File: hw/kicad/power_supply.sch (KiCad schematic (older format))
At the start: 23 parts

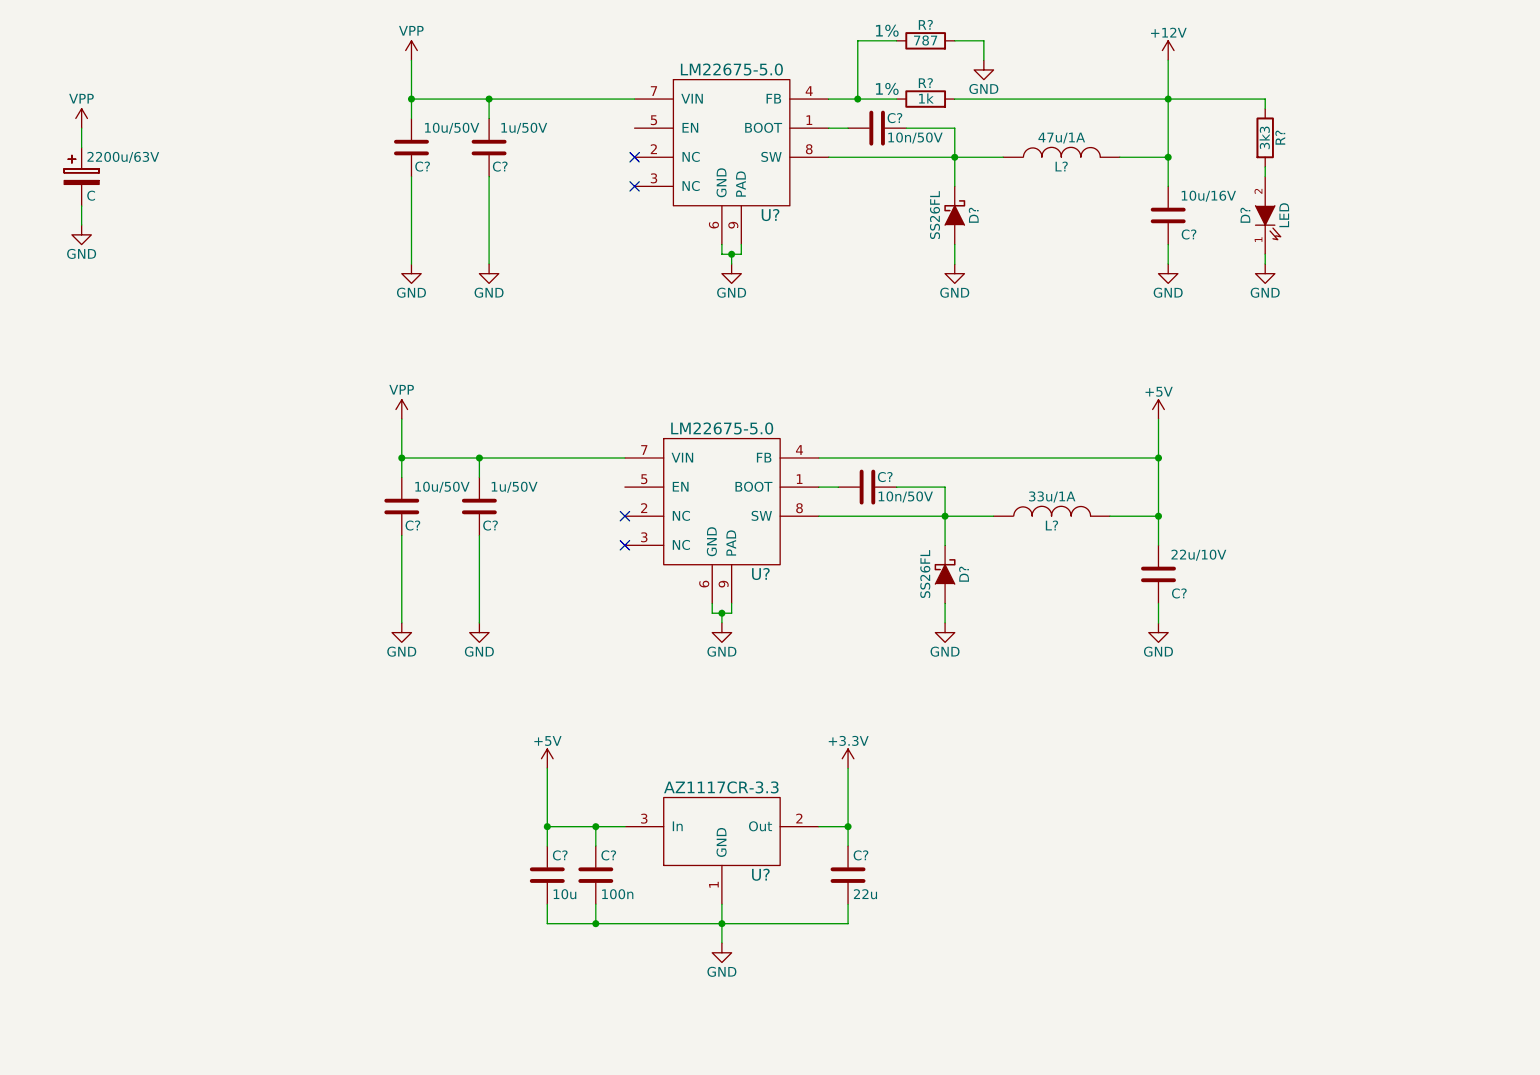
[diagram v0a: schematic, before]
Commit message: Gate power supply enabling and board temp sensor
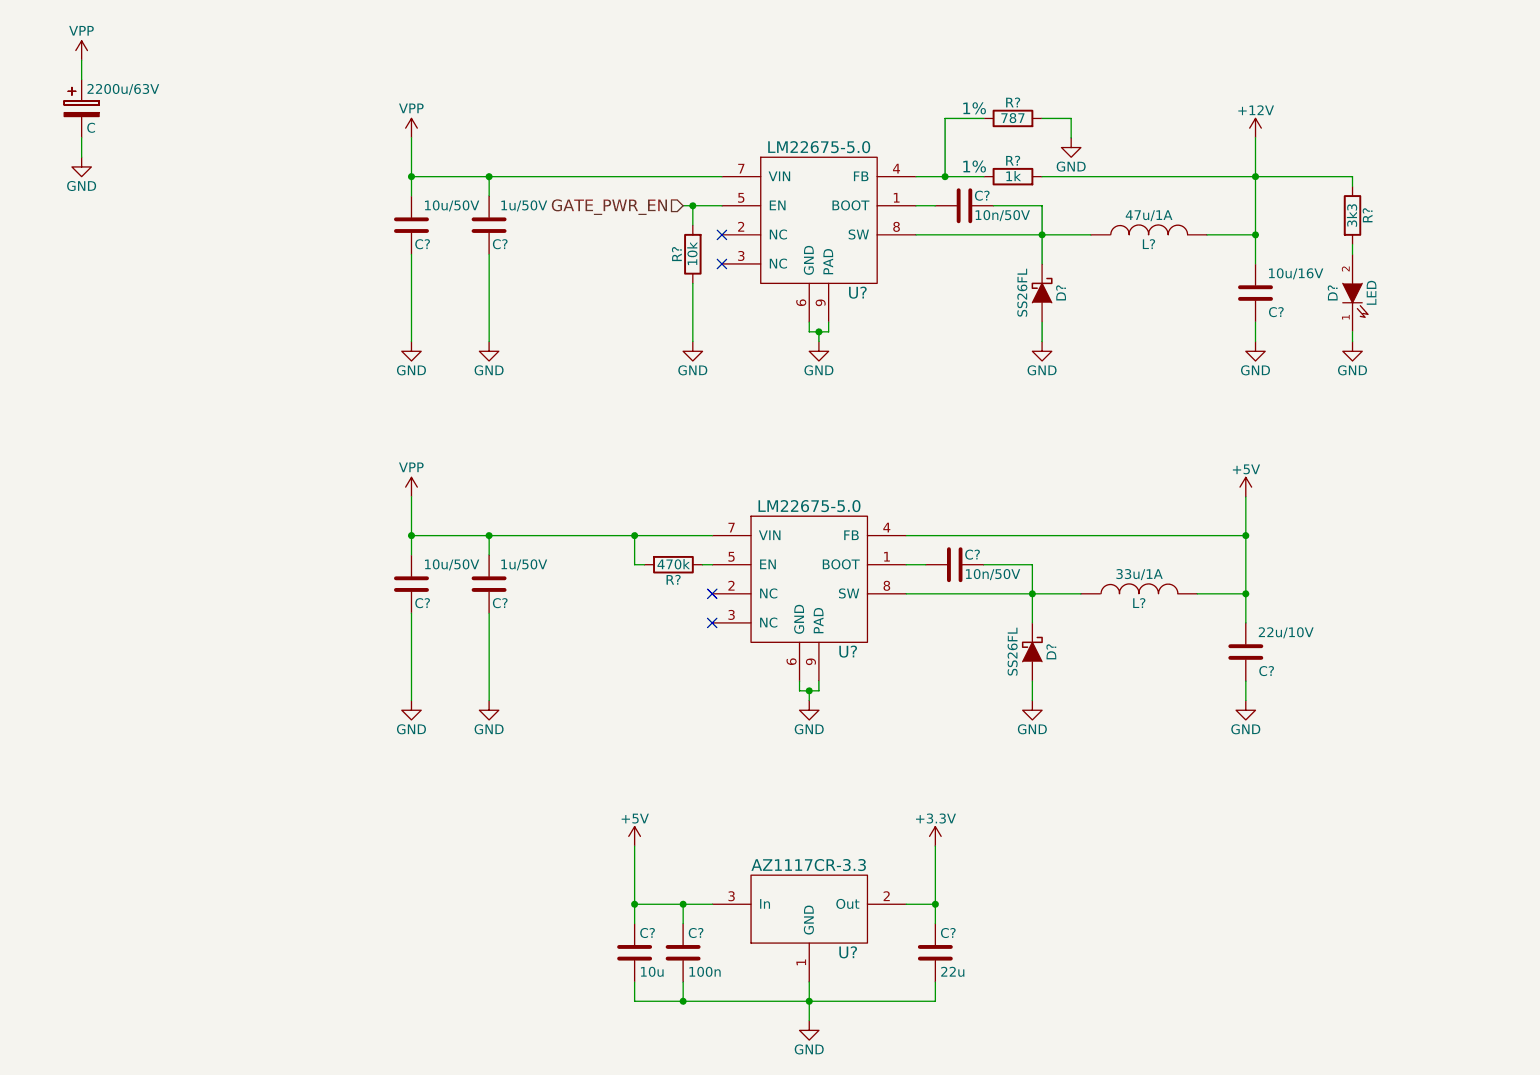
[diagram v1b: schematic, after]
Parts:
- added R?: 470k, symbol R
- added R?: 10k, symbol R
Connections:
- net GND: now also R?.1
- net VPP: now also R?.2
- net GATE_PWR_EN: now reaches U?.5 (EN)
- net GATE_PWR_EN: now also R?.2
- net at U?.5 (EN): now also R?.1
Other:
- moved on the sheet: 2200u/63V, C?, D?, L?, R?, U?

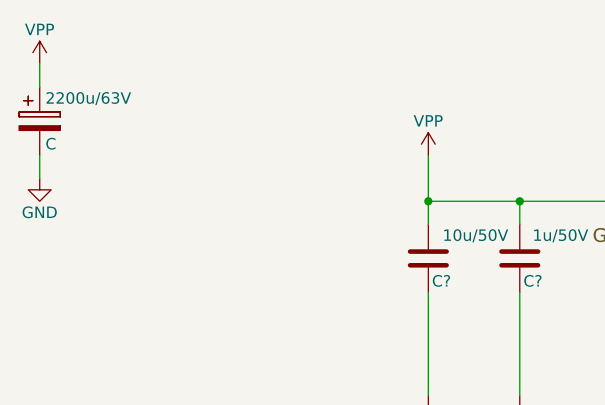
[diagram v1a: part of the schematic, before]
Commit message: TVS across bat connection
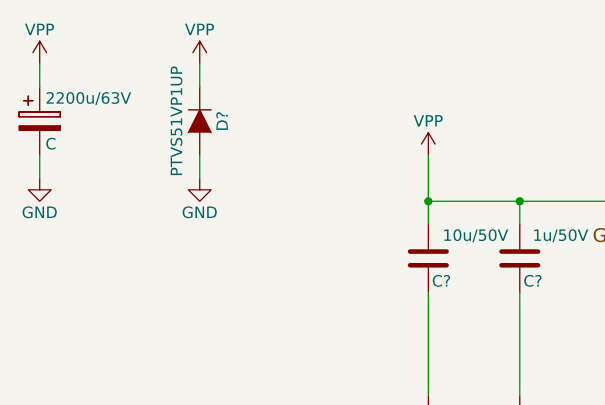
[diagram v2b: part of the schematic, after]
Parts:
- added D?: PTVS51VP1UP, SOD-128:SOD-128, symbol D
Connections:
- net GND: now also D?.2 (A)
- net VPP: now also D?.1 (K)
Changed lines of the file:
@@
 LIBS:xilinx
 LIBS:Zilog
-LIBS:drv8301
 LIBS:wslp2726
 LIBS:test
@@
 Wire Wire Line
 	4800 2600 4800 2300
+$Comp
+L D D?
+U 1 1 5834CEE1
+P 2350 1400
+F 0 "D?" H 2350 1500 50  0000 C CNN
+F 1 "PTVS51VP1UP" H 2350 1300 50  0000 C CNN
+F 2 "SOD-128:SOD-128" H 2350 1400 60  0001 C CNN
+F 3 "" H 2350 1400 60  0000 C CNN
+	1    2350 1400
+	0    1    1    0
+$EndComp
+$Comp
+L VPP #PWR?
+U 1 1 5834D11D
+P 2350 1150
+F 0 "#PWR?" H 2350 1000 50  0001 C CNN
+F 1 "VPP" H 2350 1300 50  0000 C CNN
+F 2 "" H 2350 1150 60  0000 C CNN
+F 3 "" H 2350 1150 60  0000 C CNN
+	1    2350 1150
+	1    0    0    -1
+$EndComp
+Wire Wire Line
+	2350 1250 2350 1150
+$Comp
+L GND #PWR?
+U 1 1 5834D1E3
+P 2350 1650
+F 0 "#PWR?" H 2350 1400 50  0001 C CNN
+F 1 "GND" H 2350 1500 50  0000 C CNN
+F 2 "" H 2350 1650 60  0000 C CNN
+F 3 "" H 2350 1650 60  0000 C CNN
+	1    2350 1650
+	1    0    0    -1
+$EndComp
+Wire Wire Line
+	2350 1650 2350 1550
 $EndSCHEMATC

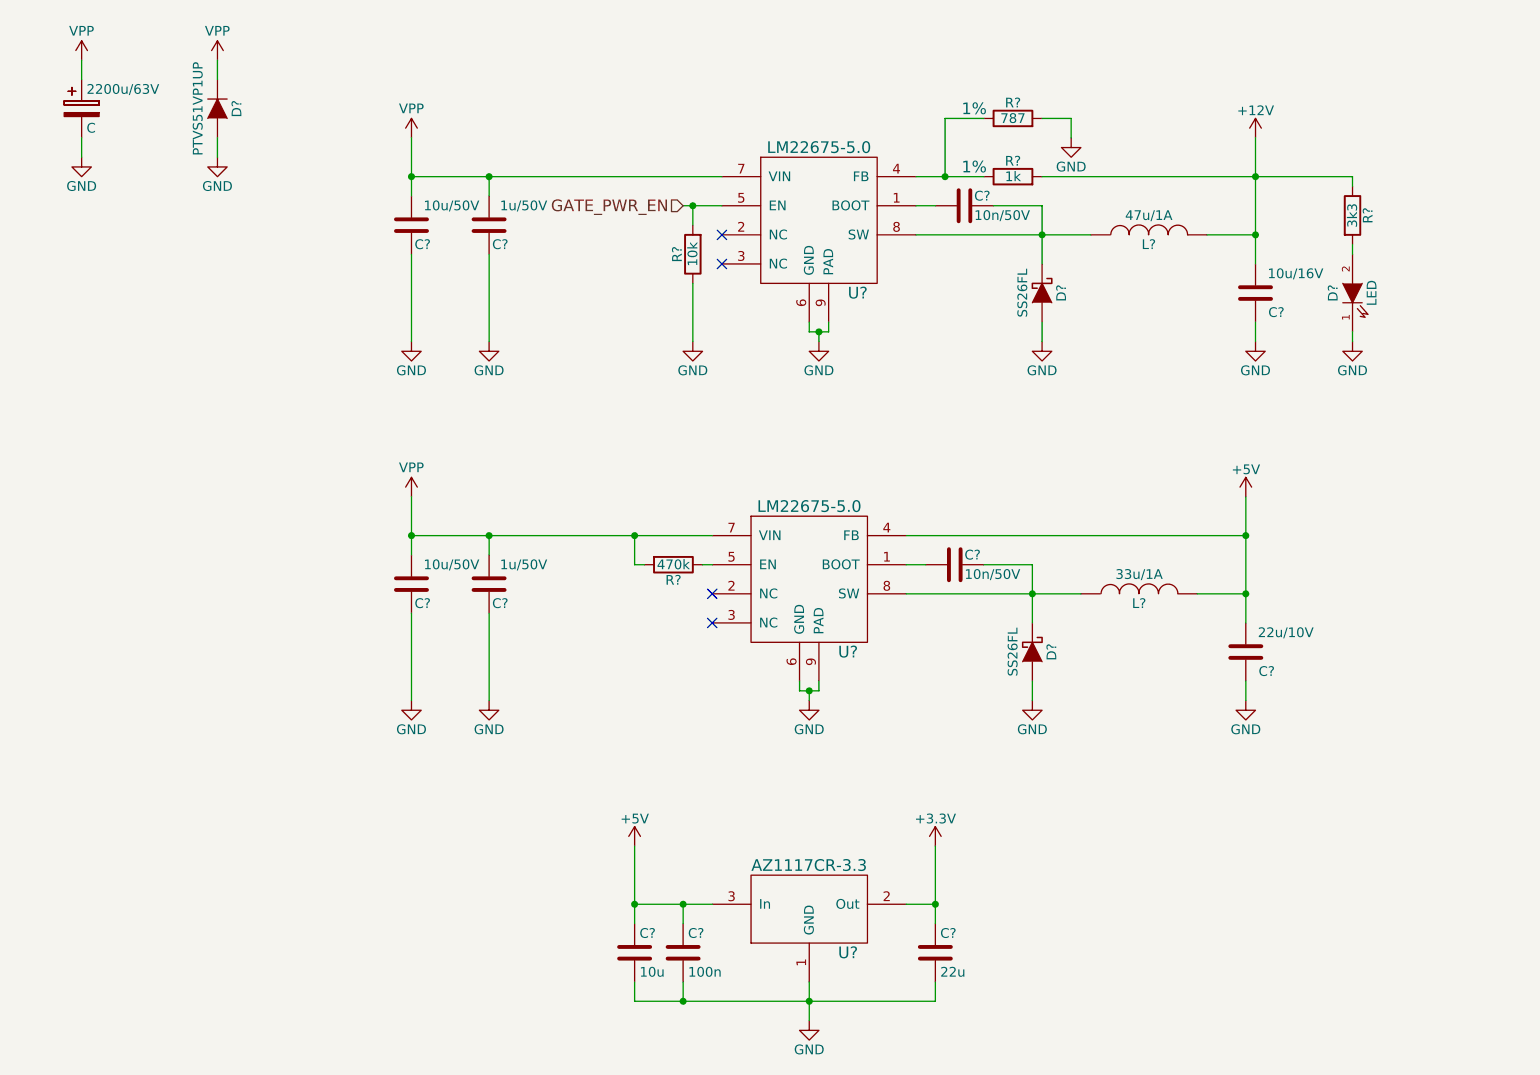
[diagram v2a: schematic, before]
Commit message: Bat pads and leds
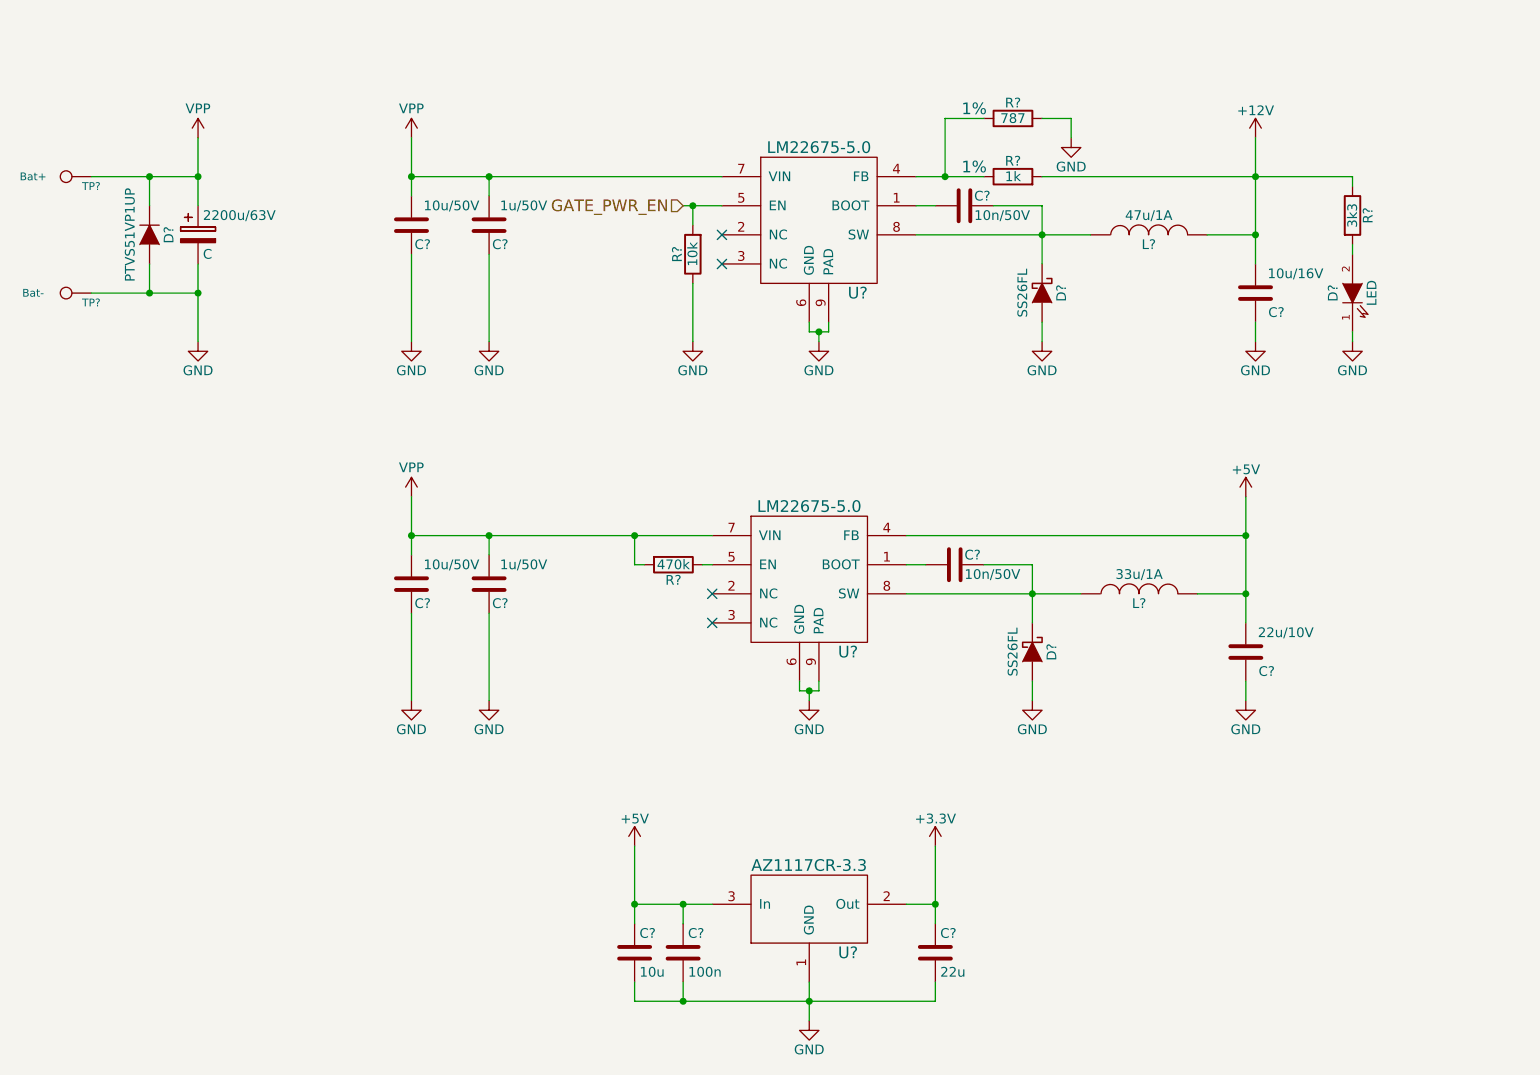
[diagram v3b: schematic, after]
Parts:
- added TP?: Bat+, Wire_Pads:SolderWirePad_single_SMD_5x10mm, symbol TESTPAD
- added TP?: Bat-, Wire_Pads:SolderWirePad_single_SMD_5x10mm, symbol TESTPAD
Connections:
- net GND: now also TP?.1
- net VPP: now also TP?.1
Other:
- moved on the sheet: 2200u/63V, D?
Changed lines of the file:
@@
 	4750 5600 4750 5500
 Wire Wire Line
-	4500 5500 4900 5500
+	4500 5500 4750 5500
+Wire Wire Line
+	4750 5500 4900 5500
 Wire Wire Line
 	5900 5500 6050 5500
 Wire Wire Line
-	6050 5200 6050 5600
-Wire Wire Line
-	5400 5900 5400 6100
-Wire Wire Line
-	4500 6000 6050 6000
+	6050 5200 6050 5500
+Wire Wire Line
+	6050 5500 6050 5600
+Wire Wire Line
+	5400 5900 5400 6000
+Wire Wire Line
+	5400 6000 5400 6100
+Wire Wire Line
+	4500 6000 4750 6000
+Wire Wire Line
+	4750 6000 5400 6000
+Wire Wire Line
+	5400 6000 6050 6000
 Wire Wire Line
 	6050 6000 6050 5900
@@
 Connection ~ 4750 6000
 Wire Wire Line
-	4500 5200 4500 5600
+	4500 5200 4500 5500
+Wire Wire Line
+	4500 5500 4500 5600
 Connection ~ 4750 5500
 Connection ~ 4500 5500
@@
 L CP 2200u/63V
 U 1 1 582A6ACE
-P 1650 1400
-F 0 "2200u/63V" H 1675 1500 50  0000 L CNN
-F 1 "C" H 1675 1300 50  0000 L CNN
-F 2 "" H 1688 1250 30  0000 C CNN
-F 3 "" H 1650 1400 60  0000 C CNN
-	1    1650 1400
+P 2250 2050
+F 0 "2200u/63V" H 2275 2150 50  0000 L CNN
+F 1 "C" H 2275 1950 50  0000 L CNN
+F 2 "" H 2288 1900 30  0000 C CNN
+F 3 "" H 2250 2050 60  0000 C CNN
+	1    2250 2050
 	1    0    0    -1
 $EndComp
@@
 L VPP #PWR?
 U 1 1 582A6B17
-P 1650 1150
-F 0 "#PWR?" H 1650 1000 50  0001 C CNN
-F 1 "VPP" H 1650 1300 50  0000 C CNN
-F 2 "" H 1650 1150 60  0000 C CNN
-F 3 "" H 1650 1150 60  0000 C CNN
-	1    1650 1150
+P 2250 1550
+F 0 "#PWR?" H 2250 1400 50  0001 C CNN
+F 1 "VPP" H 2250 1700 50  0000 C CNN
+F 2 "" H 2250 1550 60  0000 C CNN
+F 3 "" H 2250 1550 60  0000 C CNN
+	1    2250 1550
 	1    0    0    -1
 $EndComp
@@
 L GND #PWR?
 U 1 1 582A75C3
-P 1650 1650
-F 0 "#PWR?" H 1650 1400 50  0001 C CNN
-F 1 "GND" H 1650 1500 50  0000 C CNN
-F 2 "" H 1650 1650 60  0000 C CNN
-F 3 "" H 1650 1650 60  0000 C CNN
-	1    1650 1650
-	1    0    0    -1
-$EndComp
-Wire Wire Line
-	1650 1650 1650 1550
-Wire Wire Line
-	1650 1250 1650 1150
+P 2250 2600
+F 0 "#PWR?" H 2250 2350 50  0001 C CNN
+F 1 "GND" H 2250 2450 50  0000 C CNN
+F 2 "" H 2250 2600 60  0000 C CNN
+F 3 "" H 2250 2600 60  0000 C CNN
+	1    2250 2600
+	1    0    0    -1
+$EndComp
+Wire Wire Line
+	2250 2600 2250 2350
+Wire Wire Line
+	2250 2350 2250 2200
+Wire Wire Line
+	2250 1900 2250 1750
+Wire Wire Line
+	2250 1750 2250 1550
 $Comp
 L GND #PWR?
@@
 	5400 2500 5400 2550
 Wire Wire Line
-	5400 2550 5500 2550
+	5400 2550 5450 2550
+Wire Wire Line
+	5450 2550 5500 2550
 Wire Wire Line
 	5450 2550 5450 2600
@@
 $EndComp
 Wire Wire Line
-	5950 1750 6300 1750
+	5950 1750 6100 1750
+Wire Wire Line
+	6100 1750 6300 1750
 Wire Wire Line
 	6300 1450 6100 1450
@@
 	5950 1900 6050 1900
 Wire Wire Line
-	5950 2050 6850 2050
-Wire Wire Line
-	6600 1900 6600 2200
+	5950 2050 6600 2050
+Wire Wire Line
+	6600 2050 6850 2050
+Wire Wire Line
+	6600 1900 6600 2050
+Wire Wire Line
+	6600 2050 6600 2200
 Wire Wire Line
 	6600 1900 6350 1900
@@
 	7700 2050 7450 2050
 Wire Wire Line
-	7700 1550 7700 2200
+	7700 1550 7700 1750
+Wire Wire Line
+	7700 1750 7700 2050
+Wire Wire Line
+	7700 2050 7700 2200
 $Comp
 L GND #PWR?
@@
 	7700 2600 7700 2500
 Wire Wire Line
-	6600 1750 8200 1750
+	6600 1750 7700 1750
+Wire Wire Line
+	7700 1750 8200 1750
 Connection ~ 7700 2050
 $Comp
@@
 	3750 1850 3750 1750
 Wire Wire Line
-	3350 1750 4950 1750
+	3350 1750 3750 1750
+Wire Wire Line
+	3750 1750 4950 1750
 $Comp
 L C C?
@@
 $EndComp
 Wire Wire Line
-	3350 1550 3350 1850
+	3350 1550 3350 1750
+Wire Wire Line
+	3350 1750 3350 1850
 Connection ~ 3750 1750
 $Comp
@@
 	5350 4350 5350 4400
 Wire Wire Line
-	5350 4400 5450 4400
+	5350 4400 5400 4400
+Wire Wire Line
+	5400 4400 5450 4400
 Wire Wire Line
 	5400 4400 5400 4450
@@
 	5900 3750 6000 3750
 Wire Wire Line
-	5900 3900 6800 3900
-Wire Wire Line
-	6550 3750 6550 4050
+	5900 3900 6550 3900
+Wire Wire Line
+	6550 3900 6800 3900
+Wire Wire Line
+	6550 3750 6550 3900
+Wire Wire Line
+	6550 3900 6550 4050
 Wire Wire Line
 	6550 3750 6300 3750
@@
 	7650 3900 7400 3900
 Wire Wire Line
-	7650 3400 7650 4050
+	7650 3400 7650 3600
+Wire Wire Line
+	7650 3600 7650 3900
+Wire Wire Line
+	7650 3900 7650 4050
 $Comp
 L GND #PWR?
@@
 	3750 3700 3750 3600
 Wire Wire Line
-	3350 3600 4900 3600
+	3350 3600 3750 3600
+Wire Wire Line
+	3750 3600 4500 3600
+Wire Wire Line
+	4500 3600 4900 3600
 $Comp
 L C C?
@@
 $EndComp
 Wire Wire Line
-	3350 3400 3350 3700
+	3350 3400 3350 3600
+Wire Wire Line
+	3350 3600 3350 3700
 Connection ~ 3750 3600
 $Comp
@@
 GATE_PWR_EN
 Wire Wire Line
-	4750 1900 4950 1900
+	4750 1900 4800 1900
+Wire Wire Line
+	4800 1900 4950 1900
 $Comp
 L R R?
@@
 L D D?
 U 1 1 5834CEE1
-P 2350 1400
-F 0 "D?" H 2350 1500 50  0000 C CNN
-F 1 "PTVS51VP1UP" H 2350 1300 50  0000 C CNN
-F 2 "SOD-128:SOD-128" H 2350 1400 60  0001 C CNN
-F 3 "" H 2350 1400 60  0000 C CNN
-	1    2350 1400
+P 2000 2050
+F 0 "D?" H 2000 2150 50  0000 C CNN
+F 1 "PTVS51VP1UP" H 2000 1950 50  0000 C CNN
+F 2 "SOD-128:SOD-128" H 2000 2050 60  0001 C CNN
+F 3 "" H 2000 2050 60  0000 C CNN
+	1    2000 2050
 	0    1    1    0
 $EndComp
 $Comp
-L VPP #PWR?
-U 1 1 5834D11D
-P 2350 1150
-F 0 "#PWR?" H 2350 1000 50  0001 C CNN
-F 1 "VPP" H 2350 1300 50  0000 C CNN
-F 2 "" H 2350 1150 60  0000 C CNN
-F 3 "" H 2350 1150 60  0000 C CNN
-	1    2350 1150
-	1    0    0    -1
-$EndComp
-Wire Wire Line
-	2350 1250 2350 1150
-$Comp
-L GND #PWR?
-U 1 1 5834D1E3
-P 2350 1650
-F 0 "#PWR?" H 2350 1400 50  0001 C CNN
-F 1 "GND" H 2350 1500 50  0000 C CNN
-F 2 "" H 2350 1650 60  0000 C CNN
-F 3 "" H 2350 1650 60  0000 C CNN
-	1    2350 1650
-	1    0    0    -1
-$EndComp
-Wire Wire Line
-	2350 1650 2350 1550
+L TESTPAD TP?
+U 1 1 58361977
+P 1650 1750
+F 0 "TP?" V 1600 1700 40  0000 C CNN
+F 1 "Bat+" V 1650 2000 40  0000 C CNN
+F 2 "Wire_Pads:SolderWirePad_single_SMD_5x10mm" V 1650 1900 60  0001 C CNN
+F 3 "" V 1650 1900 60  0000 C CNN
+	1    1650 1750
+	0    -1   -1   0
+$EndComp
+$Comp
+L TESTPAD TP?
+U 1 1 5836197E
+P 1650 2350
+F 0 "TP?" V 1600 2300 40  0000 C CNN
+F 1 "Bat-" V 1650 2600 40  0000 C CNN
+F 2 "Wire_Pads:SolderWirePad_single_SMD_5x10mm" V 1650 2500 60  0001 C CNN
+F 3 "" V 1650 2500 60  0000 C CNN
+	1    1650 2350
+	0    -1   -1   0
+$EndComp
+Wire Wire Line
+	1700 2350 2000 2350
+Wire Wire Line
+	2000 2350 2250 2350
+Wire Wire Line
+	2000 2350 2000 2200
+Wire Wire Line
+	2000 1900 2000 1750
+Wire Wire Line
+	1700 1750 2000 1750
+Wire Wire Line
+	2000 1750 2250 1750
+Connection ~ 2250 2350
+Connection ~ 2000 2350
+Connection ~ 2250 1750
+Connection ~ 2000 1750
 $EndSCHEMATC
